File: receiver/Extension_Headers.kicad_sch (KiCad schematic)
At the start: 7 parts, among them U5 FT231XQ-R, U6 MBT3904DW1T1G

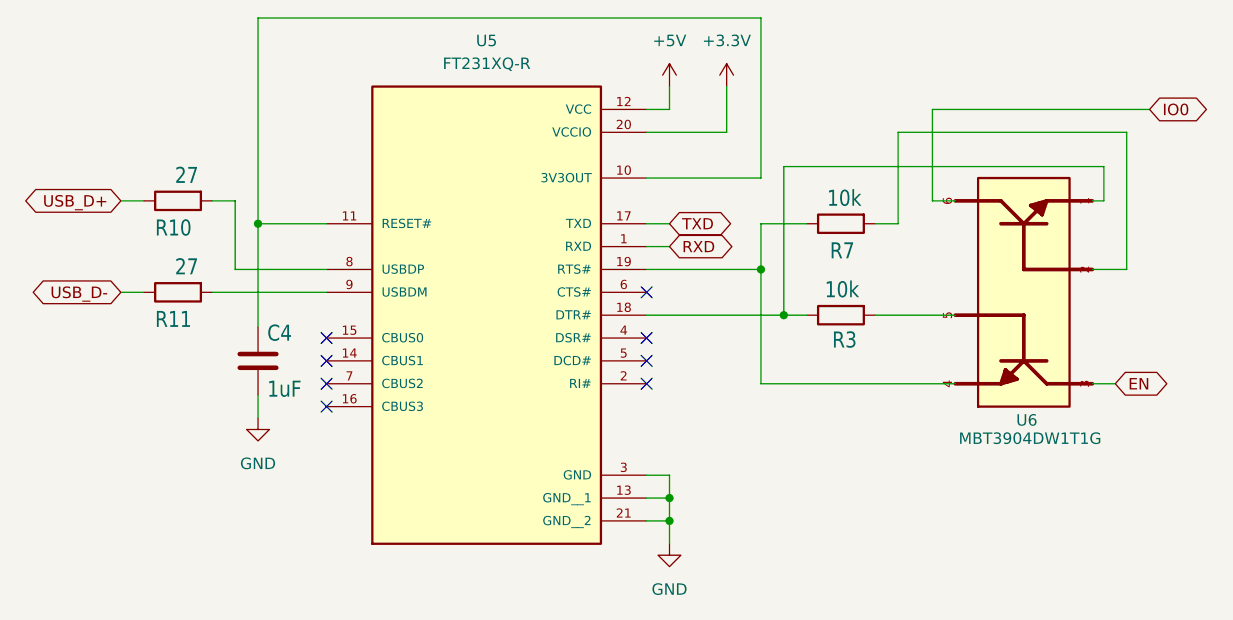
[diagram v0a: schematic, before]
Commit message: restored v1.7 of receiver, since 2.0 is abandoned
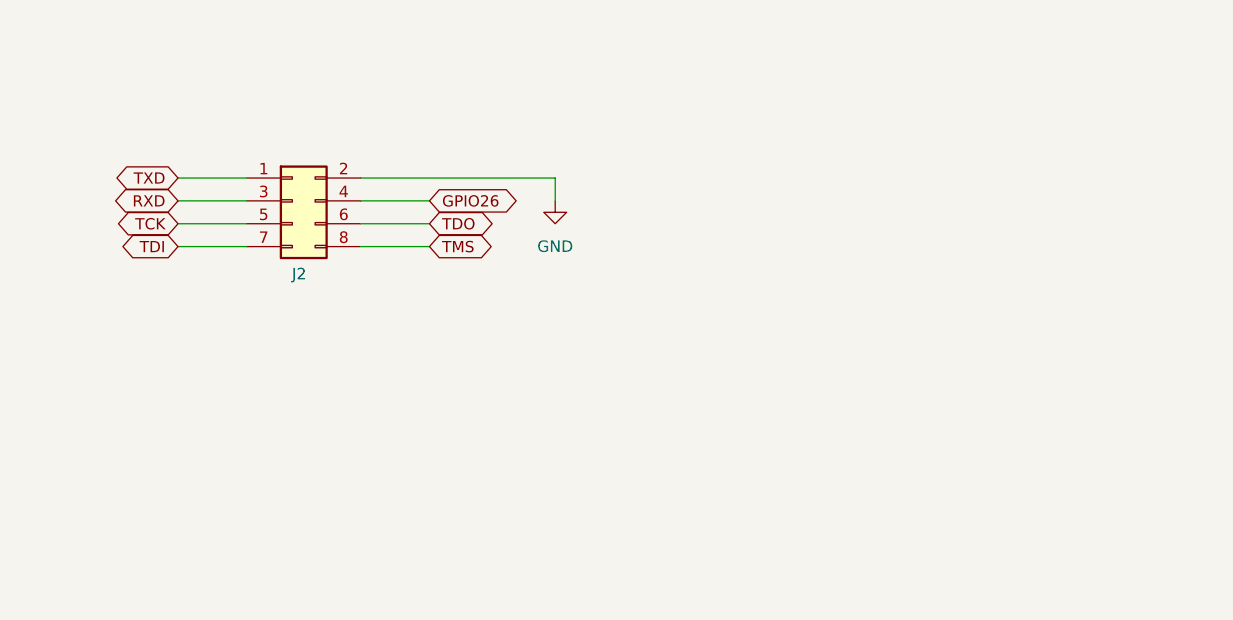
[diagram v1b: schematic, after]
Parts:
- removed C4: 1uF, receiver:C0805, symbol Device:C
- removed R10, R11: 27, Resistor_SMD:R_0805_2012Metric_Pad1.20x1.40mm_HandSolder, symbol Device:R
- removed R3, R7: 10k, Resistor_SMD:R_0805_2012Metric_Pad1.20x1.40mm_HandSolder, symbol Device:R
- removed U5: FT231XQ-R, receiver:QFN50P400X400X80-21N, symbol receiver:FT231XQ-R
- removed U6: MBT3904DW1T1G, MBT3904DW1T1G:SOT236, symbol receiver:MBT3904DW1T1G
- added J2: Conn_02x05_Counter_Clockwise, Connector_PinHeader_2.54mm:PinHeader_2x04_P2.54mm_Vertical, symbol Connector_Generic:Conn_02x04_Odd_Even
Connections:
- net GND: now also J2.2 (Pin_2)
- net RXD: now also J2.3 (Pin_3)
- net TXD: now also J2.1 (Pin_1)
- new net GPIO26: J2.4 (Pin_4)
- new net TCK: J2.5 (Pin_5)
- new net TDI: J2.7 (Pin_7)
- new net TDO: J2.6 (Pin_6)
- new net TMS: J2.8 (Pin_8)
- no-connect marks 8 -> 0
